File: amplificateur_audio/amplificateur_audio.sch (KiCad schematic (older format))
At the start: 52 parts, among them J2 Conn_01x02, J3 Conn_01x03, K1 Relay_1CT, Q1 Q_PNP_EBC, Q10 Q_PNP_BCE, Q11 BC636, Q12 Q_NPN_BCE, Q13 Q_NPN_EBC, Q2 Q_PNP_EBC, Q3 Q_PNP_EBC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

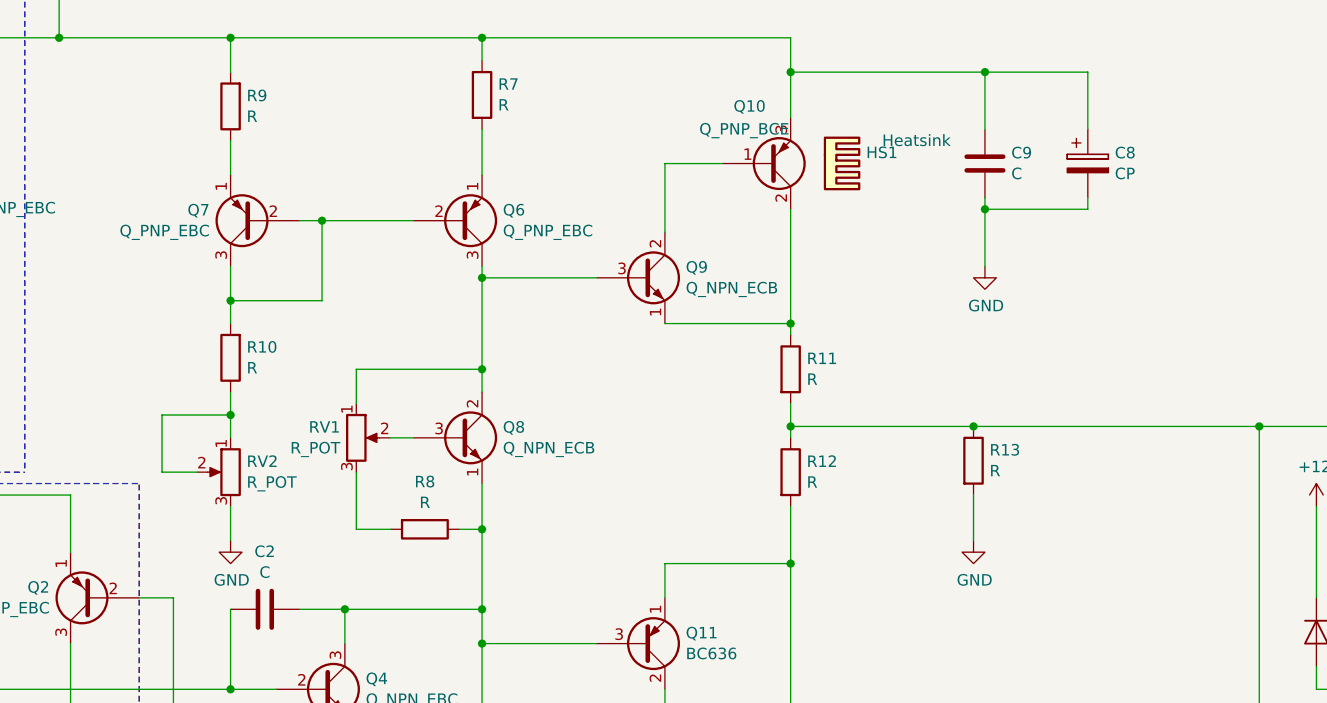
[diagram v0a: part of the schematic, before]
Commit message: replaced potentiometer with wires
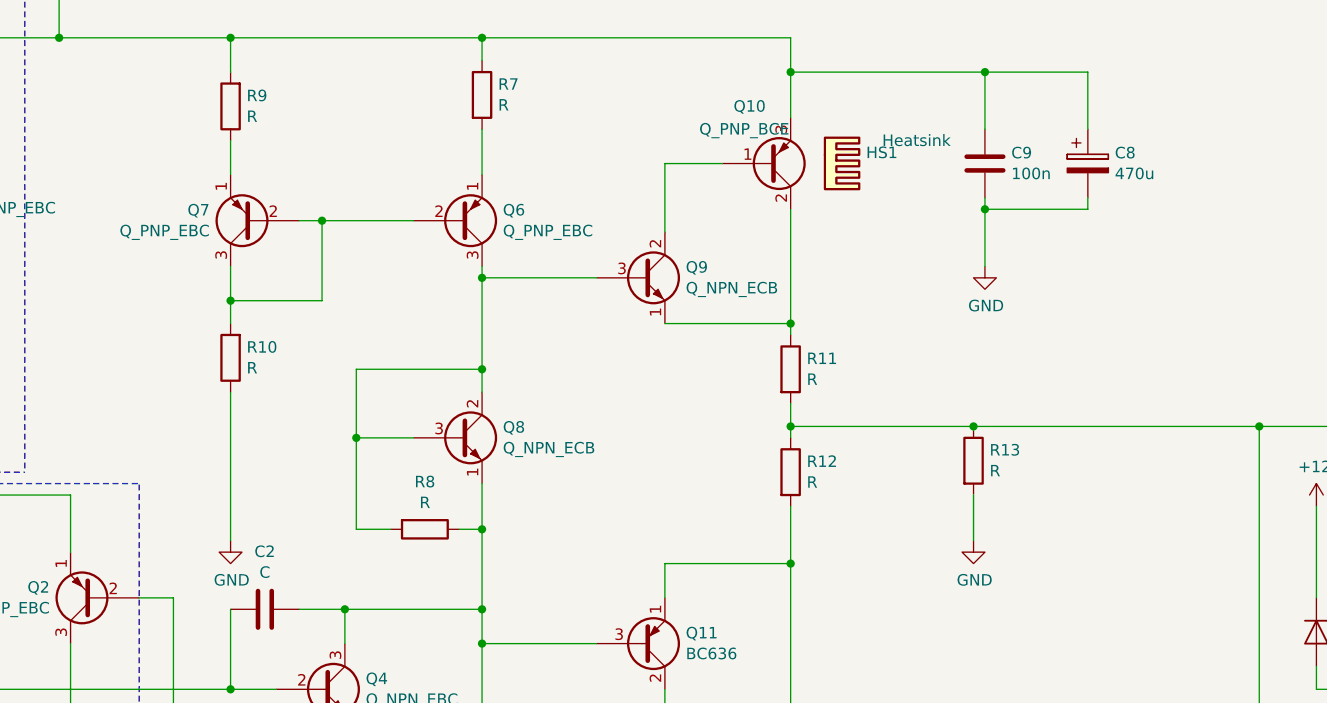
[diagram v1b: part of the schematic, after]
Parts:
- removed RV1, RV2: R_POT, symbol Device:R_POT
- C1, C3: footprint (none) -> Capacitor_THT:CP_Radial_D8.0mm_P5.00mm
- C10, C4, C6: footprint (none) -> Capacitor_THT:CP_Radial_D4.0mm_P1.50mm
- C11, C2, C5, C7: footprint (none) -> Capacitor_THT:C_Rect_L7.2mm_W3.5mm_P5.00mm_FKS2_FKP2_MKS2_MKP2
- C8: value CP -> 470u; footprint (none) -> Capacitor_THT:CP_Radial_D12.5mm_P5.00mm
- C9: value C -> 100n; footprint (none) -> Capacitor_THT:C_Rect_L7.2mm_W3.5mm_P5.00mm_FKS2_FKP2_MKS2_MKP2
- D1, D2, D3: footprint (none) -> Diode_THT:D_DO-35_SOD27_P10.16mm_Horizontal
- HS1, HS2: footprint (none) -> Heatsink:Heatsink_Fischer_SK104-STC-STIC_35x13mm_2xDrill2.5mm
- J2: footprint (none) -> Connector_Phoenix_MSTB:PhoenixContact_MSTBVA_2,5_2-G-5,08_1x02_P5.08mm_Vertical
- J3: footprint (none) -> Connector_Phoenix_MSTB:PhoenixContact_MSTBVA_2,5_3-G-5,08_1x03_P5.08mm_Vertical
- K1: footprint Relay_THT:Relay_StandexMeder_DIP_LowProfile -> be_elec_footprint:Relais_112LMH2
- Q1, Q13, Q2, Q3, Q4, Q5, Q6, Q7: footprint (none) -> Package_TO_SOT_THT:TO-18-3
- Q10, Q12: footprint (none) -> Package_TO_SOT_THT:TO-220-3_Vertical
- Q11: footprint Package_TO_SOT_THT:TO-92_Inline -> Package_TO_SOT_THT:TO-126-3_Vertical
- Q8, Q9: footprint (none) -> Package_TO_SOT_THT:TO-126-3_Vertical
- R1, R10, R13, R14, R15, R16, R17, R2, R3, R4, R5, R6, R7, R8, R9: footprint (none) -> Resistor_THT:R_Axial_DIN0207_L6.3mm_D2.5mm_P10.16mm_Horizontal
- R11, R12: footprint (none) -> Resistor_THT:R_Axial_DIN0516_L15.5mm_D5.0mm_P20.32mm_Horizontal
- U1: footprint (none) -> CmpAmpliAudio:Jack_35RAPC2AV
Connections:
- net GND: now also R10.1
- net at Q6.3 (C), Q8.2 (C), Q9.3 (B): now also Q8.3 (B), R8.2

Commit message: rectification du circuit
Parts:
- added RV1, RV2: R_POT, CmpAmpliAudio:Potentiometer_Bourns_3296W_Vertical, symbol Device:R_POT
- C1, C3: footprint Capacitor_THT:CP_Radial_D8.0mm_P5.00mm -> CmpAmpliAudio:CP_Radial_D8.0mm_P5.00mm
- C10: value CP -> 470u; footprint Capacitor_THT:CP_Radial_D4.0mm_P1.50mm -> CmpAmpliAudio:CP_Radial_D12.5mm_P5.00mm
- C11, C2, C9: footprint Capacitor_THT:C_Rect_L7.2mm_W3.5mm_P5.00mm_FKS2_FKP2_MKS2_MKP2 -> CmpAmpliAudio:C_Rect_L7.2mm_W3.5mm_P5.00mm_FKS2_FKP2_MKS2_MKP2
- C4, C6: value CP -> 10u; footprint Capacitor_THT:CP_Radial_D4.0mm_P1.50mm -> CmpAmpliAudio:C_Rect_L7.2mm_W3.5mm_P5.00mm_FKS2_FKP2_MKS2_MKP2
- C5, C7: value C -> 100n; footprint Capacitor_THT:C_Rect_L7.2mm_W3.5mm_P5.00mm_FKS2_FKP2_MKS2_MKP2 -> CmpAmpliAudio:C_Rect_L7.2mm_W3.5mm_P5.00mm_FKS2_FKP2_MKS2_MKP2
- C8: footprint Capacitor_THT:CP_Radial_D12.5mm_P5.00mm -> CmpAmpliAudio:CP_Radial_D12.5mm_P5.00mm
- D1, D2, D3: footprint Diode_THT:D_DO-35_SOD27_P10.16mm_Horizontal -> CmpAmpliAudio:D_DO-35_SOD27_P10.16mm_Horizontal
- HS1, HS2: footprint Heatsink:Heatsink_Fischer_SK104-STC-STIC_35x13mm_2xDrill2.5mm -> CmpAmpliAudio:Heatsink_Fischer_SK104-STC-STIC_35x13mm_2xDrill2.5mm
- J2: footprint Connector_Phoenix_MSTB:PhoenixContact_MSTBVA_2,5_2-G-5,08_1x02_P5.08mm_Vertical -> CmpAmpliAudio:PhoenixContact_MSTBVA_2,5_2-G-5,08_1x02_P5.08mm_Vertical
- J3: footprint Connector_Phoenix_MSTB:PhoenixContact_MSTBVA_2,5_3-G-5,08_1x03_P5.08mm_Vertical -> CmpAmpliAudio:PhoenixContact_MSTBVA_2,5_3-G-5,08_1x03_P5.08mm_Vertical
- Q1, Q13, Q2, Q3, Q4, Q5, Q6, Q7: footprint Package_TO_SOT_THT:TO-18-3 -> CmpAmpliAudio:TO-18-3
- Q10, Q12: footprint Package_TO_SOT_THT:TO-220-3_Vertical -> CmpAmpliAudio:TO-220-3_Vertical
- Q11, Q8, Q9: footprint Package_TO_SOT_THT:TO-126-3_Vertical -> CmpAmpliAudio:TO-126-3_Vertical
- R1, R10, R13, R14, R15, R16, R17, R2, R3, R4, R5, R6, R7, R8, R9: footprint Resistor_THT:R_Axial_DIN0207_L6.3mm_D2.5mm_P10.16mm_Horizontal -> CmpAmpliAudio:R_Axial_DIN0207_L6.3mm_D2.5mm_P10.16mm_Horizontal
- R11, R12: footprint Resistor_THT:R_Axial_DIN0516_L15.5mm_D5.0mm_P20.32mm_Horizontal -> CmpAmpliAudio:R_Axial_DIN0516_L15.5mm_D5.0mm_P20.32mm_Horizontal
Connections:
- net GND: now also J2.1 (Pin_1), RV2.1; no longer J2.2 (Pin_2), R10.1
- net at Q6.3 (C), Q8.2 (C), Q9.3 (B): now also RV1.1; no longer Q8.3 (B), R8.2
- net at K1.c2: now also J2.2 (Pin_2); no longer J2.1 (Pin_1)
- new net: R10.1, RV2.2, RV2.3
- new net: Q8.3 (B), RV1.2
- new net: R8.2, RV1.3
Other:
- moved on the sheet: J2

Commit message: light change - schematic
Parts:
- C4, C6: footprint CmpAmpliAudio:C_Rect_L7.2mm_W3.5mm_P5.00mm_FKS2_FKP2_MKS2_MKP2 -> CmpAmpliAudio:CP_Radial_D8.0mm_P5.00mm
- K1: footprint be_elec_footprint:Relais_112LMH2 -> CmpAmpliAudioTR:Relais_112LMH2
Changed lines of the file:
@@
 F 0 "C4" H 2418 6346 50  0000 L CNN
 F 1 "10u" H 2418 6255 50  0000 L CNN
-F 2 "CmpAmpliAudio:C_Rect_L7.2mm_W3.5mm_P5.00mm_FKS2_FKP2_MKS2_MKP2" H 2338 6150 50  0001 C CNN
+F 2 "CmpAmpliAudio:CP_Radial_D8.0mm_P5.00mm" H 2338 6150 50  0001 C CNN
 F 3 "~" H 2300 6300 50  0001 C CNN
 	1    2300 6300
@@
 F 0 "C6" H 2418 6946 50  0000 L CNN
 F 1 "10u" H 2418 6855 50  0000 L CNN
-F 2 "CmpAmpliAudio:C_Rect_L7.2mm_W3.5mm_P5.00mm_FKS2_FKP2_MKS2_MKP2" H 2338 6750 50  0001 C CNN
+F 2 "CmpAmpliAudio:CP_Radial_D8.0mm_P5.00mm" H 2338 6750 50  0001 C CNN
 F 3 "~" H 2300 6900 50  0001 C CNN
 	1    2300 6900
@@
 F 0 "K1" H 9850 2467 50  0000 C CNN
 F 1 "Relay_1CT" H 9850 2376 50  0000 C CNN
-F 2 "be_elec_footprint:Relais_112LMH2" V 8900 2550 50  0001 L CNN
+F 2 "CmpAmpliAudioTR:Relais_112LMH2" V 8900 2550 50  0001 L CNN
 F 3 "https://standexelectronics.com/wp-content/uploads/datasheet_reed_relay_DIP.pdf" V 9850 2000 50  0001 C CNN
 	1    10050 2400
@@
 	4150 2550 4150 2650
 $Comp
-L power:GND #PWR?
+L power:GND #PWR0111
 U 1 1 606BC4B2
 P 10450 2500
-F 0 "#PWR?" H 10450 2250 50  0001 C CNN
+F 0 "#PWR0111" H 10450 2250 50  0001 C CNN
 F 1 "GND" V 10455 2372 50  0000 R CNN
 F 2 "" H 10450 2500 50  0001 C CNN

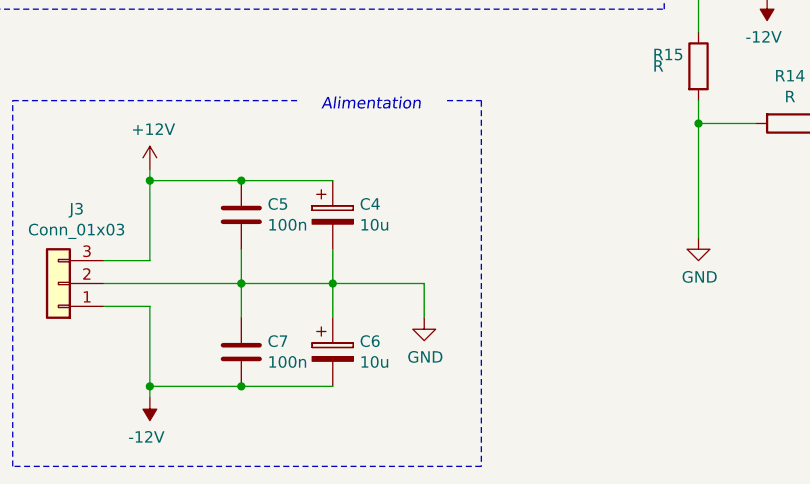
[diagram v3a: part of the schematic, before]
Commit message: schematic added 2 diodes
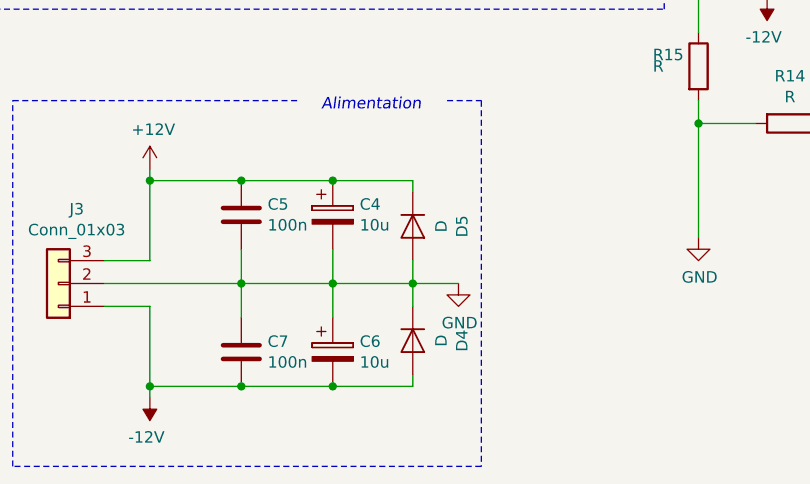
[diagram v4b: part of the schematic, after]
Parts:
- added D4, D5: D, CmpAmpliAudio:D_DO-35_SOD27_P10.16mm_Horizontal, symbol Device:D
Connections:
- net +12V: now also D5.1 (K)
- net -12V: now also D4.2 (A)
- net GND: now also D4.1 (K), D5.2 (A)
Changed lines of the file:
@@
 L power:GND #PWR0118
 U 1 1 606A2BCB
-P 2700 6750
-F 0 "#PWR0118" H 2700 6500 50  0001 C CNN
-F 1 "GND" H 2705 6577 50  0000 C CNN
-F 2 "" H 2700 6750 50  0001 C CNN
-F 3 "" H 2700 6750 50  0001 C CNN
-	1    2700 6750
+P 2850 6600
+F 0 "#PWR0118" H 2850 6350 50  0001 C CNN
+F 1 "GND" H 2855 6427 50  0000 C CNN
+F 2 "" H 2850 6600 50  0001 C CNN
+F 3 "" H 2850 6600 50  0001 C CNN
+	1    2850 6600
 	1    0    0    -1
 $EndComp
@@
 Wire Wire Line
 	1300 6600 1900 6600
-Wire Wire Line
-	2700 6600 2700 6750
 $Comp
 L Device:CP C6
@@
 Connection ~ 2300 6600
 Wire Wire Line
-	2300 6600 2700 6600
-Wire Wire Line
 	2300 6600 2300 6750
 Connection ~ 1900 6600
@@
 	0    1    1    0
 $EndComp
+$Comp
+L Device:D D5
+U 1 1 60811DD8
+P 2650 6350
+F 0 "D5" H 2650 6566 50  0000 C CNN
+F 1 "D" H 2650 6475 50  0000 C CNN
+F 2 "CmpAmpliAudio:D_DO-35_SOD27_P10.16mm_Horizontal" H 2650 6350 50  0001 C CNN
+F 3 "~" H 2650 6350 50  0001 C CNN
+	1    2650 6350
+	0    1    1    0
+$EndComp
+$Comp
+L Device:D D4
+U 1 1 6081213F
+P 2650 6850
+F 0 "D4" H 2650 7066 50  0000 C CNN
+F 1 "D" H 2650 6975 50  0000 C CNN
+F 2 "CmpAmpliAudio:D_DO-35_SOD27_P10.16mm_Horizontal" H 2650 6850 50  0001 C CNN
+F 3 "~" H 2650 6850 50  0001 C CNN
+	1    2650 6850
+	0    1    1    0
+$EndComp
+Wire Wire Line
+	2650 7000 2650 7050
+Wire Wire Line
+	2650 7050 2300 7050
+Connection ~ 2300 7050
+Wire Wire Line
+	2650 6700 2650 6600
+Wire Wire Line
+	2650 6200 2650 6150
+Wire Wire Line
+	2650 6150 2300 6150
+Connection ~ 2300 6150
+Wire Wire Line
+	2300 6600 2650 6600
+Connection ~ 2650 6600
+Wire Wire Line
+	2650 6600 2650 6500
+Wire Wire Line
+	2650 6600 2850 6600
 $EndSCHEMATC
